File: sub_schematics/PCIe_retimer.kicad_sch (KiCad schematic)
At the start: 6 parts, among them U1 SY75602ATWL-TR

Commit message: Routing small schematic fix
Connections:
- net CLK-: now reaches C5.1, U1.7 (OUT1_N)
- net CLK-: now also C2.1, U1.2 (IN_N)
- net CLK+: now reaches C4.1, U1.6 (OUT1_P)
- net CLK+: now also C1.1, U1.1 (IN_P)
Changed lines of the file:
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@@
+		)
+	)
+	(label "CLK-"
+		(at 196.85 175.26 0)
+		(effects
+			(font
+				(size 1.27 1.27)
+			)
+			(justify left bottom)
 		)
 	)
@@
 		)
 	)
+	(label "CLK+"
+		(at 196.85 172.72 0)
+		(effects
+			(font
+				(size 1.27 1.27)
+			)
+			(justify left bottom)
+		)
+	)
 	(label "PEX_RETIME.CLK-"
 		(at 212.09 180.34 0)
@@
 		)
 	)
+	(label "CLK+"
+		(at 171.45 171.45 180)
+		(effects
+			(font
+				(size 1.27 1.27)
+			)
+			(justify right bottom)
+		)
+	)
 	(label "PEX.CLK-"
 		(at 157.48 179.07 180)
+		(effects
+			(font
+				(size 1.27 1.27)
+			)
+			(justify right bottom)
+		)
+	)
+	(label "CLK-"
+		(at 171.45 173.99 180)
 		(effects
 			(font
@@
 		)
 	)
+	(rule_area
+		(exclude_from_sim no)
+		(in_bom yes)
+		(on_board yes)
+		(dnp no)
+		(polyline
+			(pts
+				(xy 167.64 168.91) (xy 170.18 168.91) (xy 170.18 180.34) (xy 167.64 180.34)
+			)
+			(stroke
+				(width 0)
+				(type dash)
+			)
+			(fill
+				(type none)
+			)
+		)
+	)
+	(rule_area
+		(exclude_from_sim no)
+		(in_bom yes)
+		(on_board yes)
+		(dnp no)
+		(polyline
+			(pts
+				(xy 212.09 167.64) (xy 214.63 167.64) (xy 214.63 182.88) (xy 212.09 182.88)
+			)
+			(stroke
+				(width 0)
+				(type dash)
+			)
+			(fill
+				(type none)
+			)
+		)
+	)
+	(rule_area
+		(exclude_from_sim no)
+		(in_bom yes)
+		(on_board yes)
+		(dnp no)
+		(polyline
+			(pts
+				(xy 198.12 166.37) (xy 200.66 166.37) (xy 200.66 181.61) (xy 198.12 181.61)
+			)
+			(stroke
+				(width 0)
+				(type dash)
+			)
+			(fill
+				(type none)
+			)
+		)
+	)
+	(netclass_flag ""
+		(length 2.54)
+		(shape round)
+		(at 199.39 166.37 0)
+		(fields_autoplaced yes)
+		(effects
+			(font
+				(size 1.27 1.27)
+			)
+			(justify left bottom)
+		)
+		(property "Net Class" "PCIe"
+			(at 200.0885 163.83 0)
+			(show_name no)
+			(do_not_autoplace no)
+			(effects
+				(font
+					(size 1.27 1.27)
+				)
+				(justify left)
+			)
+		)
+		(property "Component Class" ""
+			(at 90.17 67.31 0)
+			(hide yes)
+			(show_name no)
+			(do_not_autoplace no)
+			(effects
+				(font
+					(size 1.27 1.27)
+					(italic yes)
+				)
+			)
+		)
+	)
+	(netclass_flag ""
+		(length 2.54)
+		(shape round)
+		(at 213.36 167.64 0)
+		(fields_autoplaced yes)
+		(effects
+			(font
+				(size 1.27 1.27)
+			)
+			(justify left bottom)
+		)
+		(property "Net Class" "PCIe"
+			(at 214.0585 165.1 0)
+			(show_name no)
+			(do_not_autoplace no)
+			(effects
+				(font
+					(size 1.27 1.27)
+				)
+				(justify left)
+			)
+		)
+		(property "Component Class" ""
+			(at 104.14 68.58 0)
+			(hide yes)
+			(show_name no)
+			(do_not_autoplace no)
+			(effects
+				(font
+					(size 1.27 1.27)
+					(italic yes)
+				)
+			)
+		)
+	)
+	(netclass_flag ""
+		(length 2.54)
+		(shape round)
+		(at 168.91 180.34 180)
+		(fields_autoplaced yes)
+		(effects
+			(font
+				(size 1.27 1.27)
+			)
+			(justify right bottom)
+		)
+		(property "Net Class" "PCIe"
+			(at 169.6085 182.88 0)
+			(show_name no)
+			(do_not_autoplace no)
+			(effects
+				(font
+					(size 1.27 1.27)
+				)
+				(justify left)
+			)
+		)
+		(property "Component Class" ""
+			(at 59.69 81.28 0)
+			(hide yes)
+			(show_name no)
+			(do_not_autoplace no)
+			(effects
+				(font
+					(size 1.27 1.27)
+					(italic yes)
+				)
+			)
+		)
+	)

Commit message: Preparing order
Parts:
- C1, C2, C4, C5: JLCPCB Part # (none) -> C20040658; MPN (none) -> 885012004001
- C3: JLCPCB Part # (none) -> C6839882; MPN (none) -> 885012105020
- U1: JLCPCB Part # (none) -> C3613417; MPN (none) -> SY75602ATWL-TR
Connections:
- net CLK+ renamed CLKIN+
- net CLKIN+: no longer C4.1, U1.6 (OUT1_P)
- net CLK- renamed CLKIN-
- net CLKIN-: no longer C5.1, U1.7 (OUT1_N)
- new net CLKOUT+: C4.1, U1.6 (OUT1_P)
- new net CLKOUT-: C5.1, U1.7 (OUT1_N)
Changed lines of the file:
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@@
 		)
 	)
-	(label "CLK-"
+	(label "CLKOUT-"
 		(at 196.85 175.26 0)
 		(effects
@@
 		)
 	)
-	(label "CLK+"
+	(label "CLKOUT+"
 		(at 196.85 172.72 0)
 		(effects
@@
 		)
 	)
-	(label "CLK+"
+	(label "CLKIN+"
 		(at 171.45 171.45 180)
 		(effects
@@
 		)
 	)
-	(label "CLK-"
+	(label "CLKIN-"
 		(at 171.45 173.99 180)
 		(effects
@@
 			)
 		)
+		(property "JLCPCB Part #" "C20040658"
+			(at 205.74 180.34 0)
+			(hide yes)
+			(show_name no)
+			(do_not_autoplace no)
+			(effects
+				(font
+					(size 1.27 1.27)
+				)
+			)
+		)
+		(property "MPN" "885012004001"
+			(at 205.74 180.34 0)
+			(hide yes)
+			(show_name no)
+			(do_not_autoplace no)
+			(effects
+				(font
+					(size 1.27 1.27)
+				)
+			)
+		)
 		(pin "2"
 		)
@@
 			)
 		)
+		(property "JLCPCB Part #" "C20040658"
+			(at 205.74 172.72 0)
+			(hide yes)
+			(show_name no)
+			(do_not_autoplace no)
+			(effects
+				(font
+					(size 1.27 1.27)
+				)
+			)
+		)
+		(property "MPN" "885012004001"
+			(at 205.74 172.72 0)
+			(hide yes)
+			(show_name no)
+			(do_not_autoplace no)
+			(effects
+				(font
+					(size 1.27 1.27)
+				)
+			)
+		)
 		(pin "2"
 		)
@@
 			)
 		)
+		(property "JLCPCB Part #" "C20040658"
+			(at 162.56 171.45 0)
+			(hide yes)
+			(show_name no)
+			(do_not_autoplace no)
+			(effects
+				(font
+					(size 1.27 1.27)
+				)
+			)
+		)
+		(property "MPN" "885012004001"
+			(at 162.56 171.45 0)
+			(hide yes)
+			(show_name no)
+			(do_not_autoplace no)
+			(effects
+				(font
+					(size 1.27 1.27)
+				)
+			)
+		)
 		(pin "2"
 		)
@@
 			)
 		)
+		(property "JLCPCB Part #" "C6839882"
+			(at 165.1 167.64 0)
+			(hide yes)
+			(show_name no)
+			(do_not_autoplace no)
+			(effects
+				(font
+					(size 1.27 1.27)
+				)
+			)
+		)
+		(property "MPN" "885012105020"
+			(at 165.1 167.64 0)
+			(hide yes)
+			(show_name no)
+			(do_not_autoplace no)
+			(effects
+				(font
+					(size 1.27 1.27)
+				)
+			)
+		)
 		(pin "1"
 		)
@@
 			)
 		)
+		(property "JLCPCB Part #" "C20040658"
+			(at 162.56 179.07 0)
+			(hide yes)
+			(show_name no)
+			(do_not_autoplace no)
+			(effects
+				(font
+					(size 1.27 1.27)
+				)
+			)
+		)
+		(property "MPN" "885012004001"
+			(at 162.56 179.07 0)
+			(hide yes)
+			(show_name no)
+			(do_not_autoplace no)
+			(effects
+				(font
+					(size 1.27 1.27)
+				)
+			)
+		)
 		(pin "2"
 		)
@@
 			(at 184.15 170.18 0)
 			(hide yes)
+			(show_name no)
+			(do_not_autoplace no)
+			(effects
+				(font
+					(size 1.27 1.27)
+				)
+			)
+		)
+		(property "JLCPCB Part #" "C3613417"
+			(at 184.15 170.18 0)
+			(hide yes)
+			(show_name no)
+			(do_not_autoplace no)
+			(effects
+				(font
+					(size 1.27 1.27)
+				)
+			)
+		)
+		(property "MPN" "SY75602ATWL-TR"
+			(at 184.15 170.18 0)
+			(hide yes)

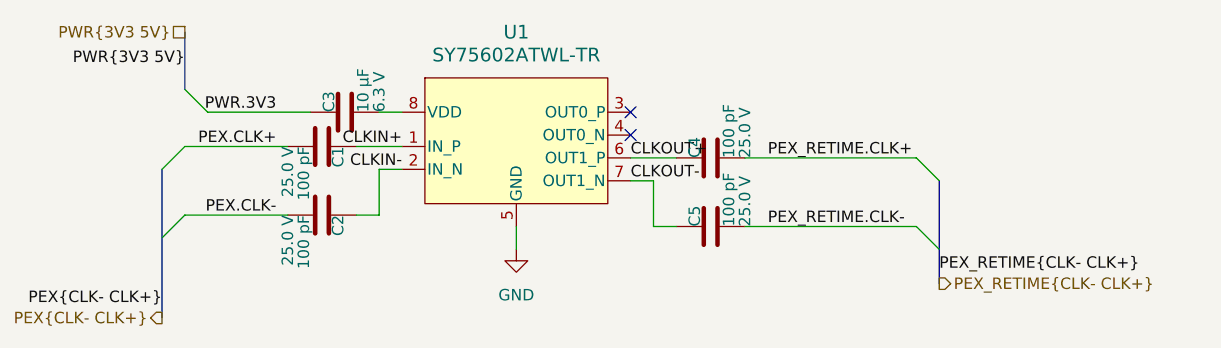
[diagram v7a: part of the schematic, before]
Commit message: Reskew changed skematics
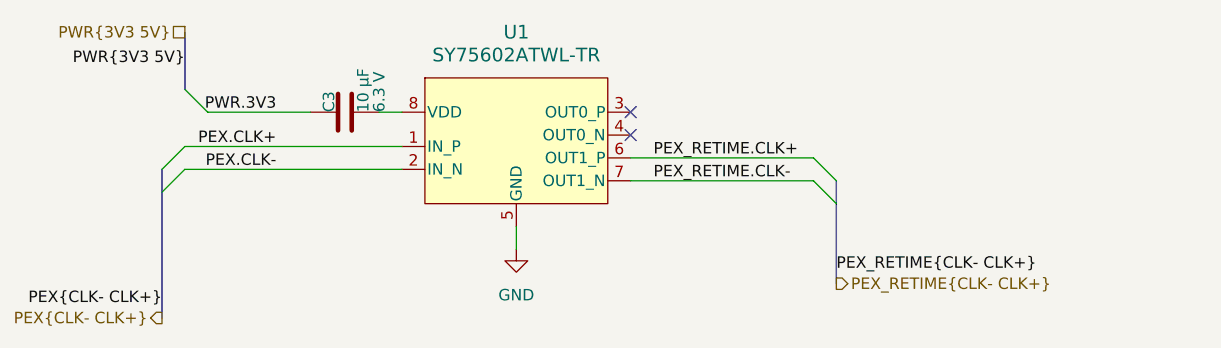
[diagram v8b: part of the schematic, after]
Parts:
- removed C1, C2, C4, C5: 0201_885012004001, WE_WCAP-CSGP:C_Wurth_WCAP-CSGP-0201, symbol WE_WCAP-CSGP:0201_885012004001
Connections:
- net CLKIN+ is gone; now on net PEX.CLK+: U1.1 (IN_P)
- net CLKIN- is gone; now on net PEX.CLK-: U1.2 (IN_N)
- net CLKOUT+ is gone; now on net PEX_RETIME.CLK+: U1.6 (OUT1_P)
- net CLKOUT- is gone; now on net PEX_RETIME.CLK-: U1.7 (OUT1_N)
